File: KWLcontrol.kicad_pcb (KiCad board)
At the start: 2 copper layers, 56.4 x 38.5 mm, 33 parts, among them J2 Conn_01x03_Socket, J3 Conn_01x03, J4 2059-323/998-403, U1 ESP32-WROOM-32, U2 TPS62172DSG, U3 TPS62172DSG, U4 TXS0101DBV

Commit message: minor changes and improvements
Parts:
- added R9: 1M, Resistor_SMD:R_0805_2012Metric_Pad1.20x1.40mm_HandSolder, F.Cu at (142.0, 129.0)
- moved C9 7.68 mm to (144.8, 110.3), turned to -90 degrees
- moved R4 5.29 mm to (146.6, 119.4)
- moved C3 4.20 mm to (146.6, 114.1), turned to -90 degrees
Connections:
- C3 pad 1: +3.3V -> Net-(U1-EN)
- PS1 pad 10: (no net) -> /AC_PE
- PS1 pad 11: (no net) -> /AC_PE
- PS1 pad 12: (no net) -> /AC_PE
- PS1 pad 13: (no net) -> /AC_PE
- PS1 pad 15: (no net) -> GNDREF
- PS1 pad 17: (no net) -> GNDREF
- PS1 pad 22: (no net) -> GNDREF
- PS1 pad 24: (no net) -> GNDREF
- PS1 pad 26: (no net) -> GNDREF
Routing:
- net /AC_PE: track 0.00 -> 30.3 mm, vias 1 -> 6
- net Net-(U1-EN): track 2.29 -> 8.81 mm
- net +3.3V: track 56.8 -> 55.1 mm
- net +12V: track 42.6 -> 41.4 mm
- net +5V: track 13.8 -> 14.9 mm
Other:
- board text added: "ESPHome ventilation system control V2 Martin Schütz ms@mschuetz.com"
- board text removed: "ESPHome home ventilation system control V1 Dr. Martin Schütz ms@mschuetz.com"

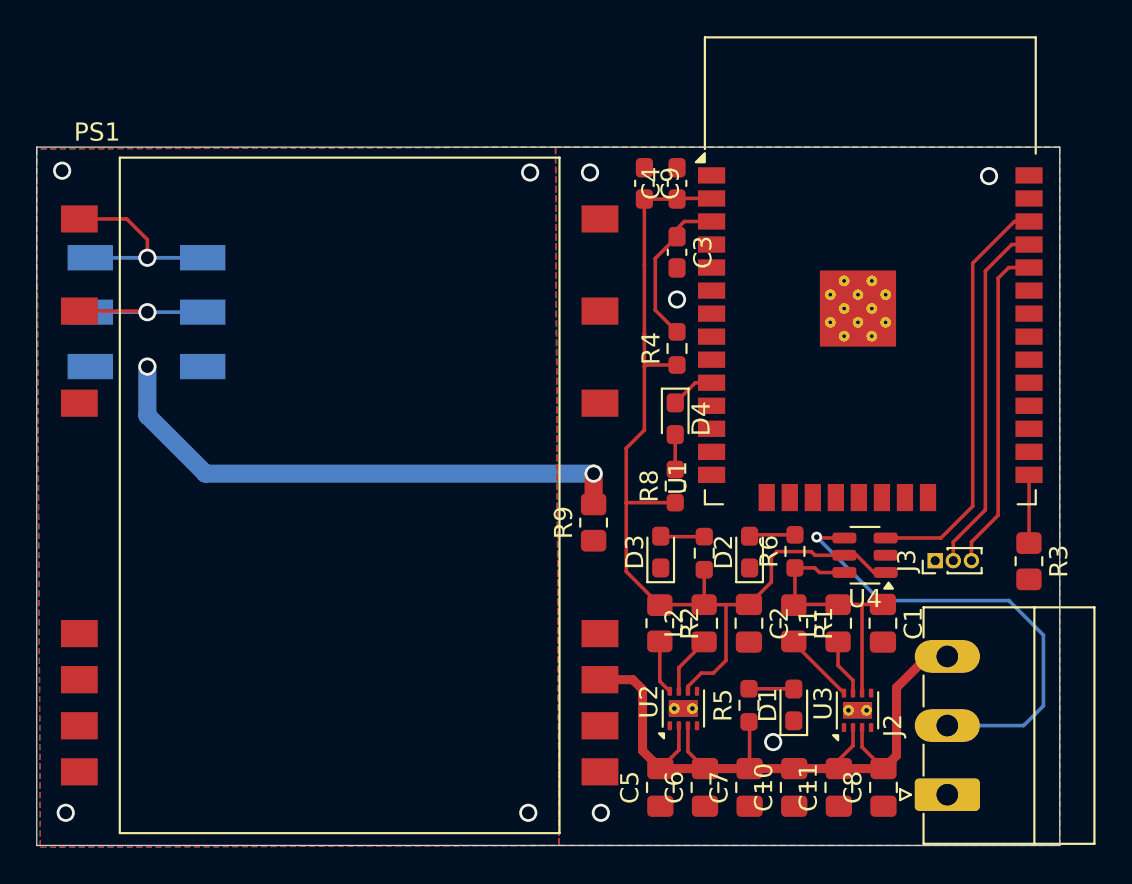
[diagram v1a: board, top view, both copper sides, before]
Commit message: improvements, add BME680
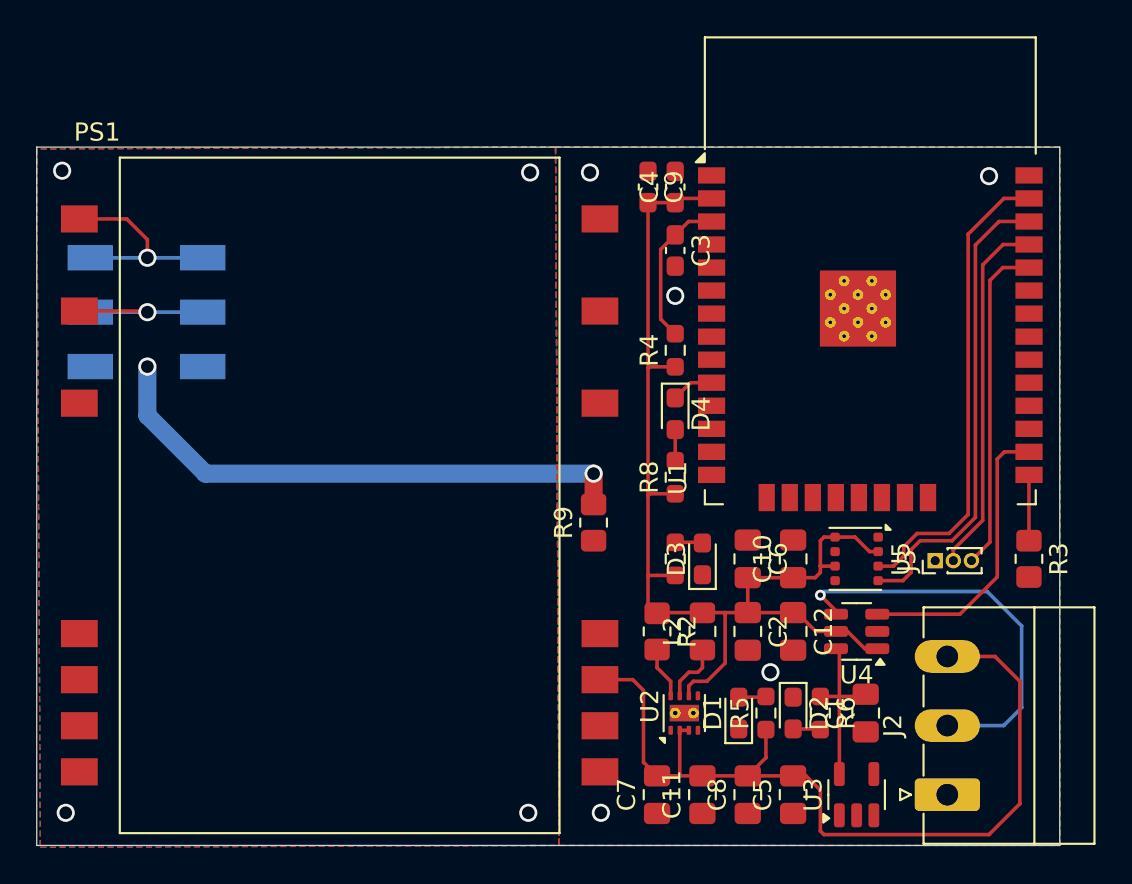
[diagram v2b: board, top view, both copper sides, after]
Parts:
- removed L1: 2.2uF, Inductor_SMD:L_0805_2012Metric_Pad1.15x1.40mm_HandSolder
- removed R1: 100k, Resistor_SMD:R_0805_2012Metric_Pad1.20x1.40mm_HandSolder
- added C12: 100n, Capacitor_SMD:C_0805_2012Metric_Pad1.18x1.45mm_HandSolder, F.Cu at (153.0, 135.0)
- added U5: BME680, Package_LGA:Bosch_LGA-8_3x3mm_P0.8mm_ClockwisePinNumbering, F.Cu at (156.5, 131.0)
- C1: value 22uF -> 2.2uF
- C10: value 1n -> 100n
- C5: value 10u -> 1u
- U3: value TPS62172DSG -> TPS76950; footprint Package_SON:WSON-8-1EP_2x2mm_P0.5mm_EP0.9x1.6mm_ThermalVias -> Package_TO_SOT_SMD:SOT-23-5
- moved C6 12.8 mm to (150.5, 131.0), turned to -90 degrees
- moved C10 12.6 mm to (153.0, 131.0)
- moved D2 9.19 mm to (153.0, 139.5), turned to -90 degrees
- moved R6 9.02 mm to (154.5, 139.5), turned to -90 degrees
- moved C11 7.53 mm to (148.0, 144.0)
- moved C8 7.49 mm to (150.5, 144.0)
- moved C5 7.33 mm to (153.0, 144.0)
- moved C7 5.12 mm to (145.5, 144.0)
- moved C1 5.04 mm to (157.0, 139.5), turned to 90 degrees
- moved U3 4.65 mm to (156.5, 144.0)
- moved U4 4.23 mm to (156.5, 135.0)
- moved D1 3.07 mm to (150.0, 139.5)
- moved D3 2.33 mm to (148.0, 131.0)
- moved R7 1.63 mm to (146.5, 131.0)
- moved R5 1.03 mm to (151.5, 139.5)
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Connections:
- C1 pad 1: +5V -> GNDREF
- C1 pad 2: GNDREF -> +5V
- C10 pad 1: GNDREF -> +3.3V
- C10 pad 2: +12V -> GNDREF
- C6 pad 2: +12V -> +3.3V
- U1 pad 26: unconnected-(U1-IO4-Pad26) -> /FAN_PWM
- U1 pad 36: /FAN_PWM -> /SCL
- U1 pad 37: unconnected-(U1-IO23-Pad37) -> /SDA
- U3 pad 1: GNDREF -> +12V
- U3 pad 2: +12V -> GNDREF
- U3 pad 4: GNDREF -> unconnected-(U3-NC-Pad4)
- U3 pad 5: GNDREF -> +5V
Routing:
- net /SDA: track 0.00 -> 26.1 mm
- net /SCL: track 0.00 -> 26.0 mm
- net +12V: track 41.4 -> 49.9 mm
- net /FAN_PWM: track 23.0 -> 15.9 mm
- net +3.3V: track 55.1 -> 62.1 mm
- net +5V: track 14.9 -> 9.72 mm
- net Net-(U3-PG): track 3.99 -> 0.00 mm
- net Net-(J2-Pin_2): track 25.9 -> 22.4 mm
- net Net-(U3-SW): track 3.17 -> 0.00 mm
- net Net-(D2-A): track 2.53 -> 1.52 mm
- net Net-(D1-A): track 2.48 -> 1.52 mm
- net Net-(D3-A): track 2.41 -> 1.52 mm
